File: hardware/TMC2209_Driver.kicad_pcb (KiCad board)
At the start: 2 copper layers, 36.7 x 39.4 mm, 29 parts, among them J1 PCIe_Stepper, J2 Conn_01x04_Male, U1 TMC2209-LA, U2 74LVC1G06, U3 24LC02

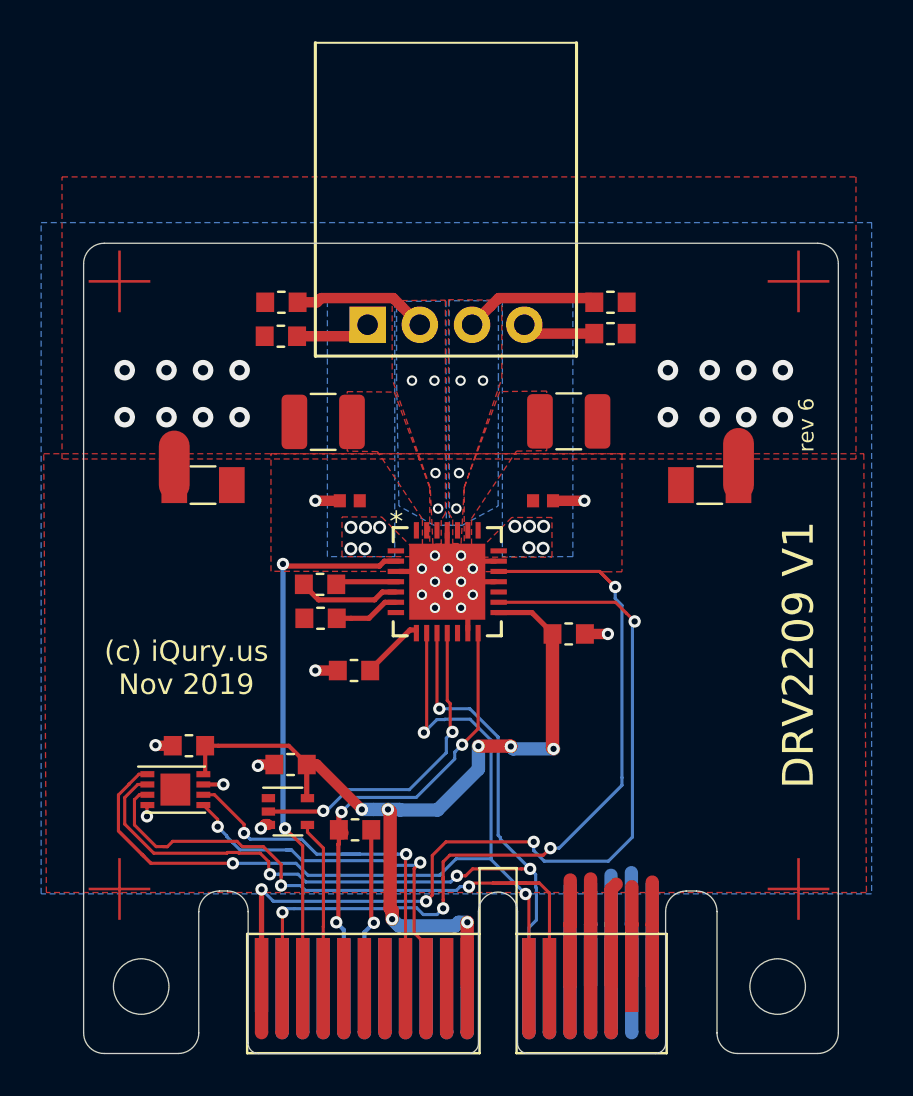
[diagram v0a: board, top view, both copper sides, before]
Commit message: Add electrolytic cap to the driver.
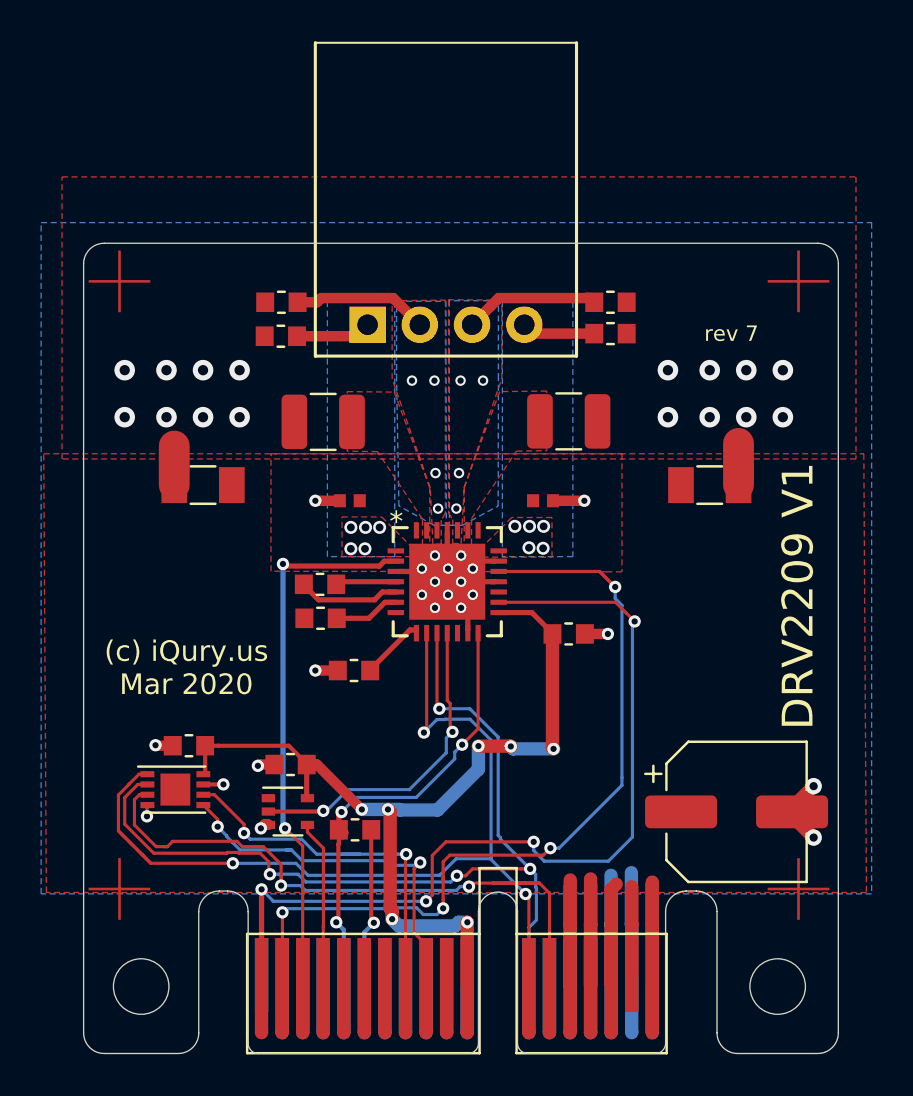
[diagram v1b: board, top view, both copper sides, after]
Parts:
- added C15: 100uV 35V, Capacitor_SMD:CP_Elec_6.3x7.7, F.Cu at (140.8, 102.2)
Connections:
- U3 pad 9: (no net) -> GND
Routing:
- net GND: track 48.6 -> 52.0 mm, vias 37 -> 39
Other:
- board text added: "(c) iQury.us Mar 2020"
- board text added: "rev 7"
- board text removed: "(c) iQury.us Nov 2019"
- board text removed: "rev 6"

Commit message: Add mouning holes to the 2209 driver.
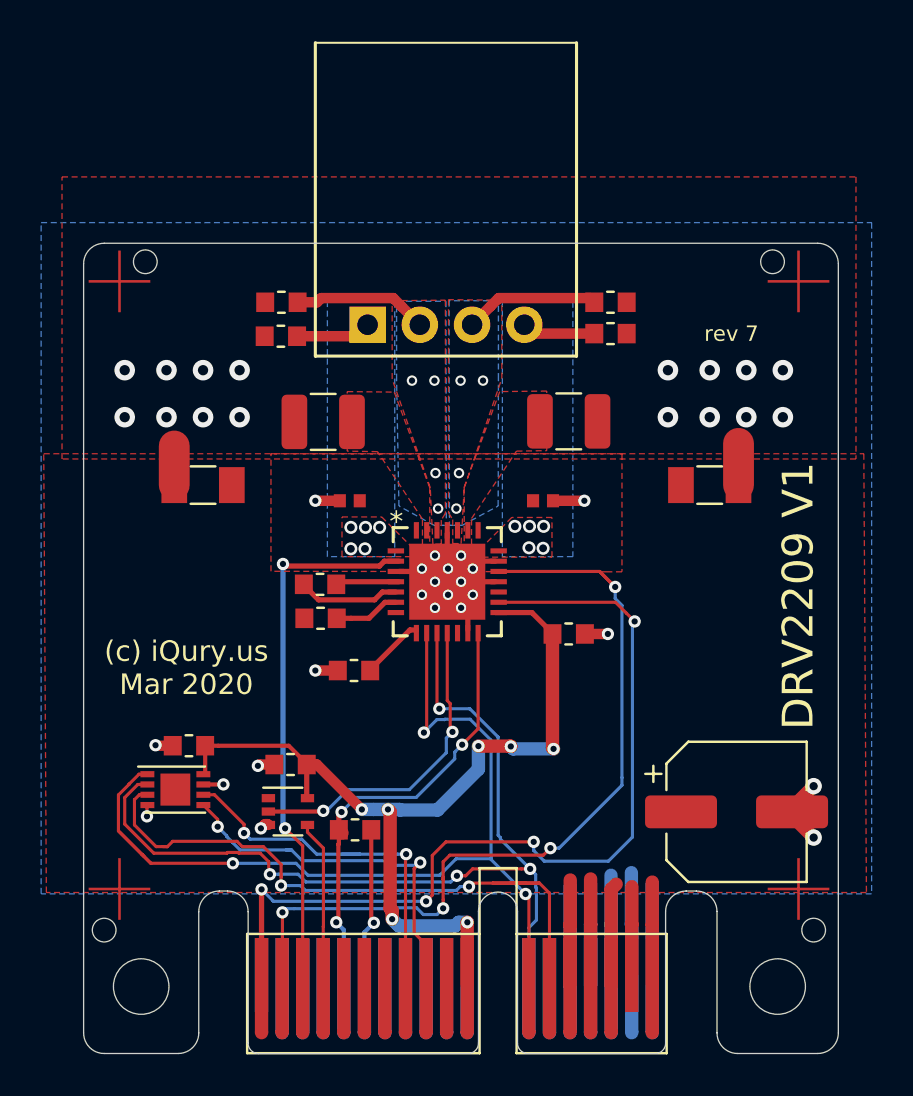
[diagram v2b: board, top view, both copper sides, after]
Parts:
- added H3: ToolingHole, PrntrBoardV2:JLC_Tool_hole, F.Cu at (112.0, 75.5)
- added H4: ToolingHole, PrntrBoardV2:JLC_Tool_hole, F.Cu at (110.0, 108.0)
- added H5: ToolingHole, PrntrBoardV2:JLC_Tool_hole, F.Cu at (142.5, 75.5)
- added H6: ToolingHole, PrntrBoardV2:JLC_Tool_hole, F.Cu at (144.5, 108.0)
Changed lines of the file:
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@@
     (drawings 33)
     (tracks 434)
-    (modules 30)
+    (modules 34)
     (nets 26)
   )
@@
   )
   (setup
-    (last_trace_width 0.65)
+    (last_trace_width 0.25)
     (user_trace_width 0.1524)
     (user_trace_width 0.2032)
@@
     (pad_to_mask_clearance 0.051)
     (solder_mask_min_width 0.25)
-    (aux_axis_origin 0 0)
+    (aux_axis_origin 109 114)
     (visible_elements FFFFFF7F)
     (pcbplotparams
@@
     (uvia_dia 0.3)
     (uvia_drill 0.1)
-    (add_net "/5V")
     (add_net "/ALARM1")
-    (add_net "/ALARM2")
-    (add_net "/CFG1")
-    (add_net "/CFG2")
-    (add_net "/CFG3")
-    (add_net "/CFG4")
     (add_net "/DIAG")
     (add_net "/DIR")
@@
     (add_net "/ID_1")
     (add_net "/ID_2")
-    (add_net "/ID_3")
-    (add_net "/MISO")
-    (add_net "/MOSI")
     (add_net "/MOTA1")
     (add_net "/MOTA2")
@@
     (add_net "/MOTB2")
     (add_net "/RX")
-    (add_net "/SCK")
     (add_net "/SCL")
     (add_net "/SDA")
     (add_net "/STEP")
     (add_net "/TX")
-    (add_net "/VREF")
     (add_net "/V_MOTORS")
-    (add_net "/~CS")
     (add_net "/~ENABLE")
-    (add_net "/~RESET")
-    (add_net "/~SLEEP")
     (add_net "GND")
     (add_net "Net-(C2-Pad2)")
@@
     (add_net "Net-(R2-Pad2)")
     (add_net "Net-(R3-Pad2)")
-    (add_net "Net-(U1-Pad12)")
-    (add_net "Net-(U1-Pad17)")
-    (add_net "Net-(U1-Pad7)")
     (add_net "VCC")
   )
+  (module "PrntrBoardV2:JLC_Tool_hole" (layer "F.Cu")
+    (at 144.5 108)
+    (fp_text reference "H6" (at 0 0.5 unlocked) (layer "F.SilkS") hide
+      (effects (font (size 1 1) (thickness 0.15)))
+    )
+    (fp_text value "ToolingHole" (at 0 -0.5 unlocked) (layer "F.Fab")
+      (effects (font (size 1 1) (thickness 0.15)))
+    )
+    (pad "" np_thru_hole circle (at 0 0) (size 1.152 1.152) (drill 1.152) (layers *.Cu *.Mask)
+      (solder_mask_margin 0.148) (clearance 0.148))
+  )
+  (module "PrntrBoardV2:JLC_Tool_hole" (layer "F.Cu")
+    (at 142.5 75.5)
+    (fp_text reference "H5" (at 0 0.5 unlocked) (layer "F.SilkS") hide
+      (effects (font (size 1 1) (thickness 0.15)))
+    )
+    (fp_text value "ToolingHole" (at 0 -0.5 unlocked) (layer "F.Fab")
+      (effects (font (size 1 1) (thickness 0.15)))
+    )
+    (pad "" np_thru_hole circle (at 0 0) (size 1.152 1.152) (drill 1.152) (layers *.Cu *.Mask)
+      (solder_mask_margin 0.148) (clearance 0.148))
+  )
+  (module "PrntrBoardV2:JLC_Tool_hole" (layer "F.Cu")
+    (at 110 108)
+    (fp_text reference "H4" (at 0 0.5 unlocked) (layer "F.SilkS") hide
+      (effects (font (size 1 1) (thickness 0.15)))
+    )
+    (fp_text value "ToolingHole" (at 0 -0.5 unlocked) (layer "F.Fab")
+      (effects (font (size 1 1) (thickness 0.15)))
+    )
+    (pad "" np_thru_hole circle (at 0 0) (size 1.152 1.152) (drill 1.152) (layers *.Cu *.Mask)
+      (solder_mask_margin 0.148) (clearance 0.148))
+  )
+  (module "PrntrBoardV2:JLC_Tool_hole" (layer "F.Cu")
+    (at 112 75.5)
+    (fp_text reference "H3" (at 0 0.5 unlocked) (layer "F.SilkS") hide
+      (effects (font (size 1 1) (thickness 0.15)))
+    )
+    (fp_text value "ToolingHole" (at 0 -0.5 unlocked) (layer "F.Fab")
+      (effects (font (size 1 1) (thickness 0.15)))
+    )
+    (pad "" np_thru_hole circle (at 0 0) (size 1.152 1.152) (drill 1.152) (layers *.Cu *.Mask)
+      (solder_mask_margin 0.148) (clearance 0.148))
+  )
   (module "Capacitor_SMD:CP_Elec_6.3x7.7" (layer "F.Cu")

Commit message: Remove the mounting holes from the 2209 driver. SHould be used on a panel.
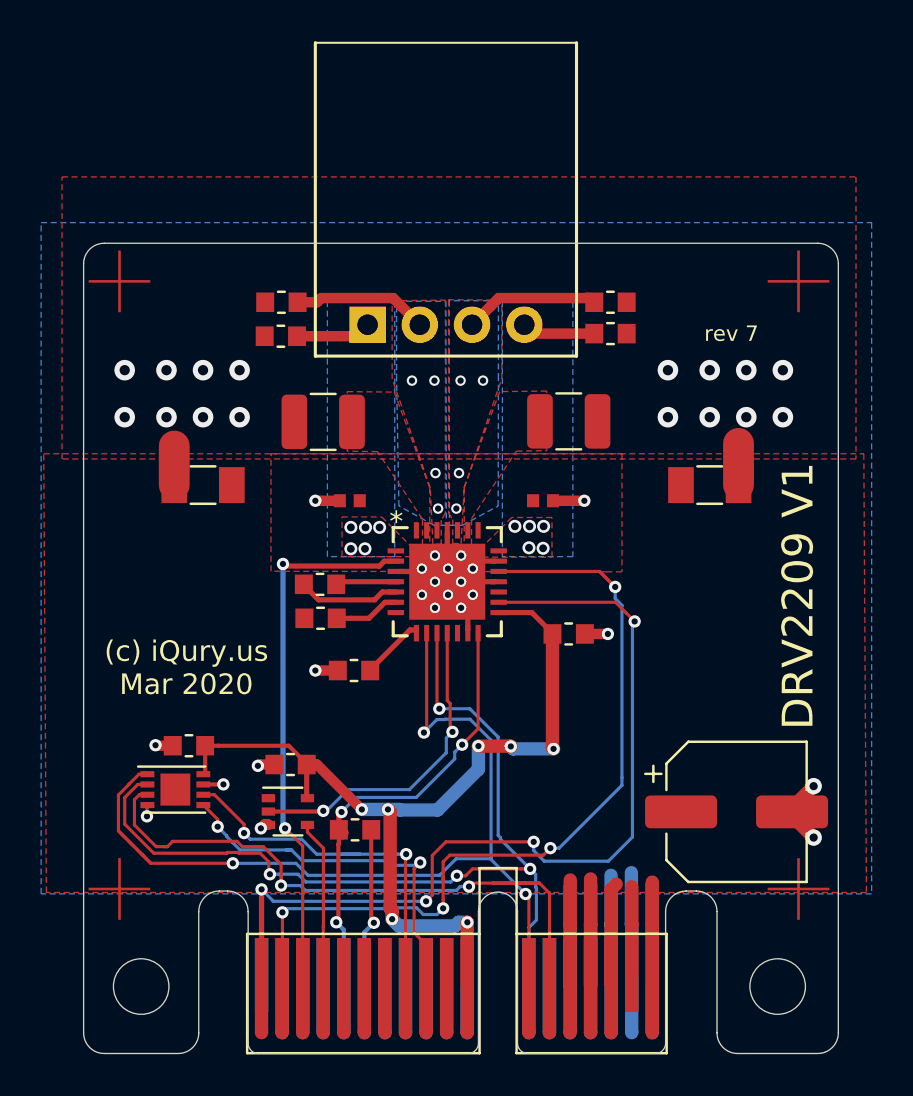
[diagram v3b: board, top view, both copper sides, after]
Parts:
- removed H3, H4, H5, H6: ToolingHole, PrntrBoardV2:JLC_Tool_hole

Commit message: Re-generate TMC2209 gerbers. Have to update the JPC component info.
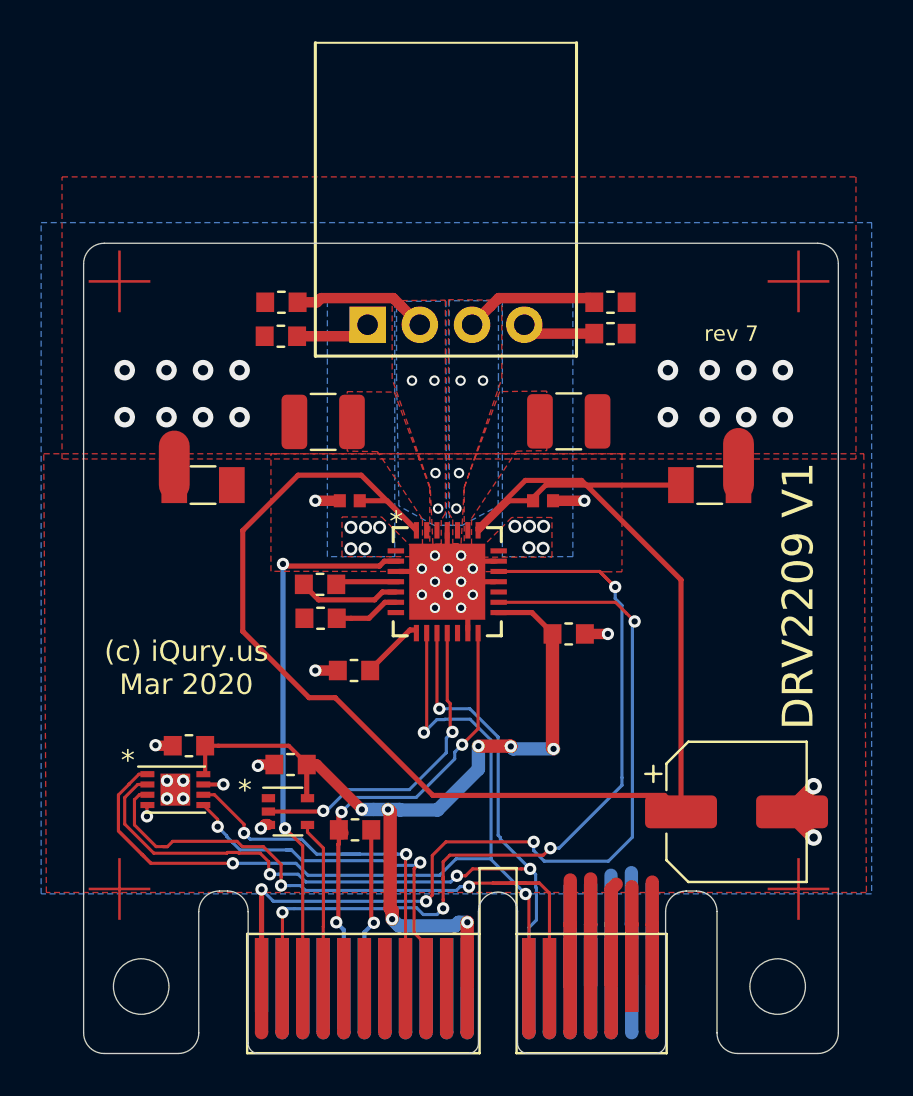
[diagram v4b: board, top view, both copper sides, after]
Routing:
- net /V_MOTORS: track 24.6 -> 103.6 mm
- net GND: vias 39 -> 43
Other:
- board text added: "*"

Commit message: Updated driver PCBs.
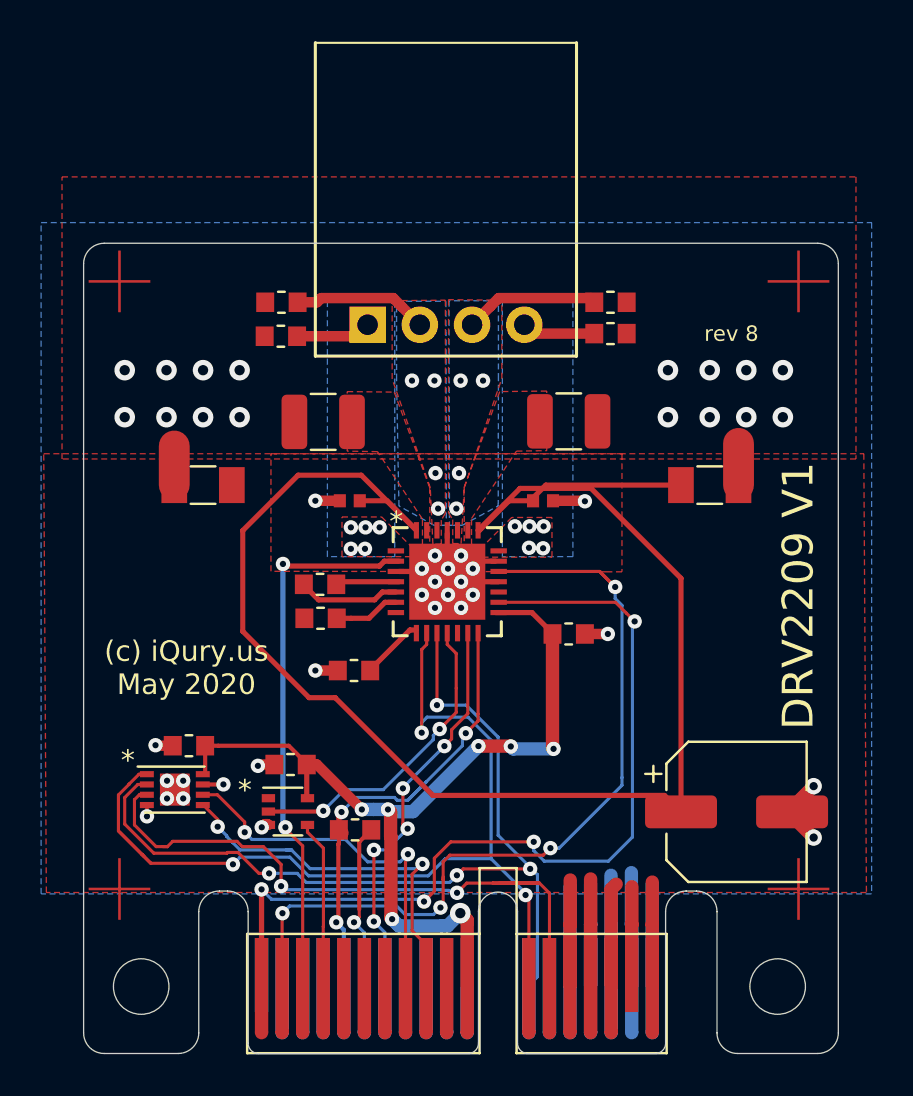
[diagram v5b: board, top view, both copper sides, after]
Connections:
- J1 pad A7: (no net) -> /CLOCK
- U1 pad 13: GND -> /CLOCK
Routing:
- net /CLOCK: track 0.00 -> 19.8 mm, vias 0 -> 5
- net /ID_2: track 32.4 -> 34.6 mm
- net /RX: track 22.1 -> 23.1 mm
- net /ID_0: track 46.9 -> 47.8 mm
- net GND: track 52.0 -> 51.2 mm
- net /DIAG: track 16.1 -> 15.5 mm
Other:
- rule via_min_size: 0.508 -> 0.7
- board text added: "(c) iQury.us May 2020"
- board text added: "rev 8"
- board text removed: "(c) iQury.us Mar 2020"
- board text removed: "rev 7"

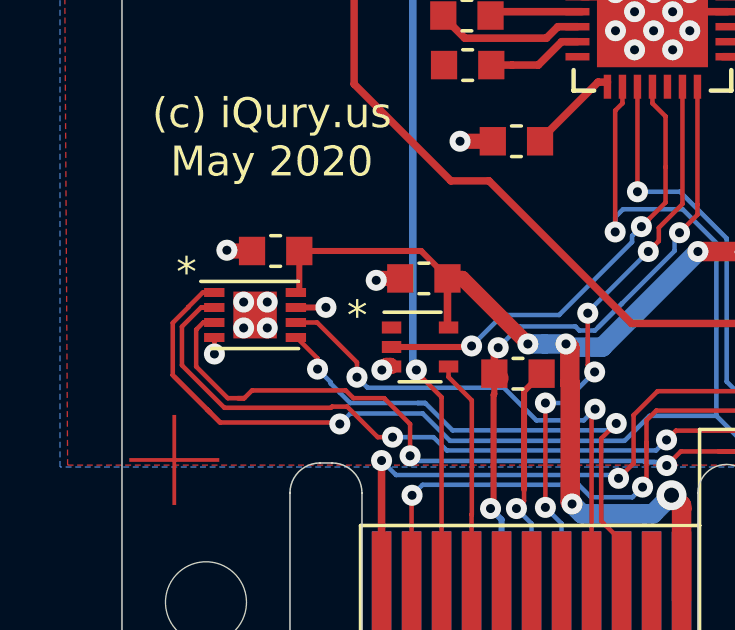
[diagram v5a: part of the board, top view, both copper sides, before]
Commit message: Update to the latest daily Kicad. Fix board outline issue on PrntrBoardV2.
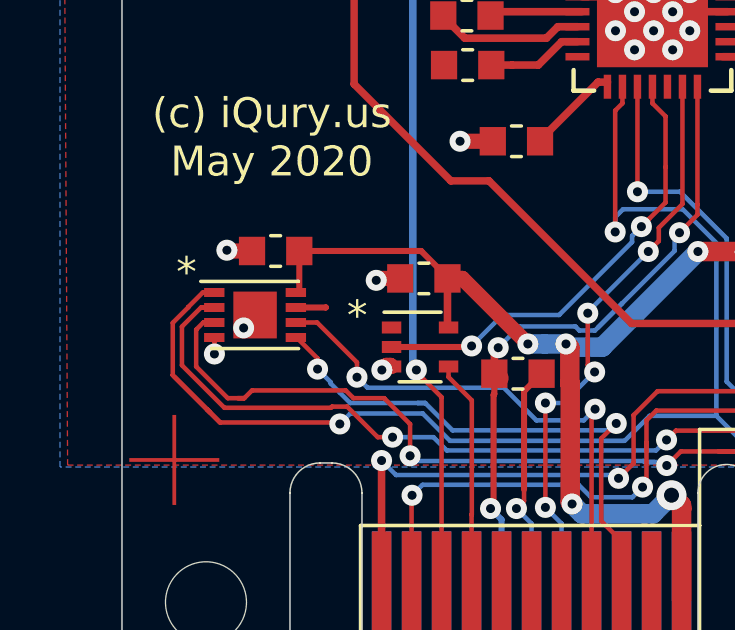
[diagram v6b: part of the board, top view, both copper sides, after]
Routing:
- net GND: vias 43 -> 39
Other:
- net class Default removed
